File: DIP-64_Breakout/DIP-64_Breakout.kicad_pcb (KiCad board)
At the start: 2 copper layers, 42.2 x 85.1 mm, 6 parts, among them J1 DIP-64 Socket, J2 Left, J3 Right, J4 Decoupling Capacitor, J5 +5V In, J6 GND In

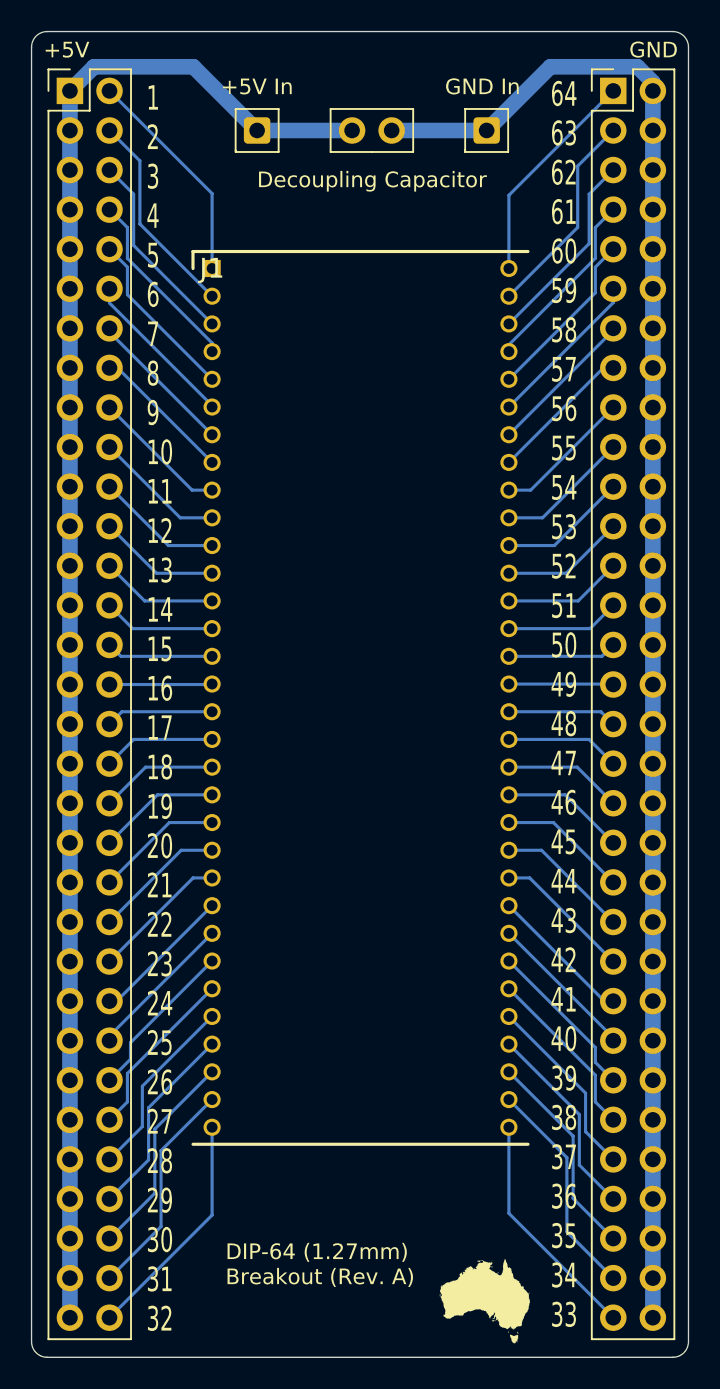
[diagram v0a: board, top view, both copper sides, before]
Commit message: Modified power input pins
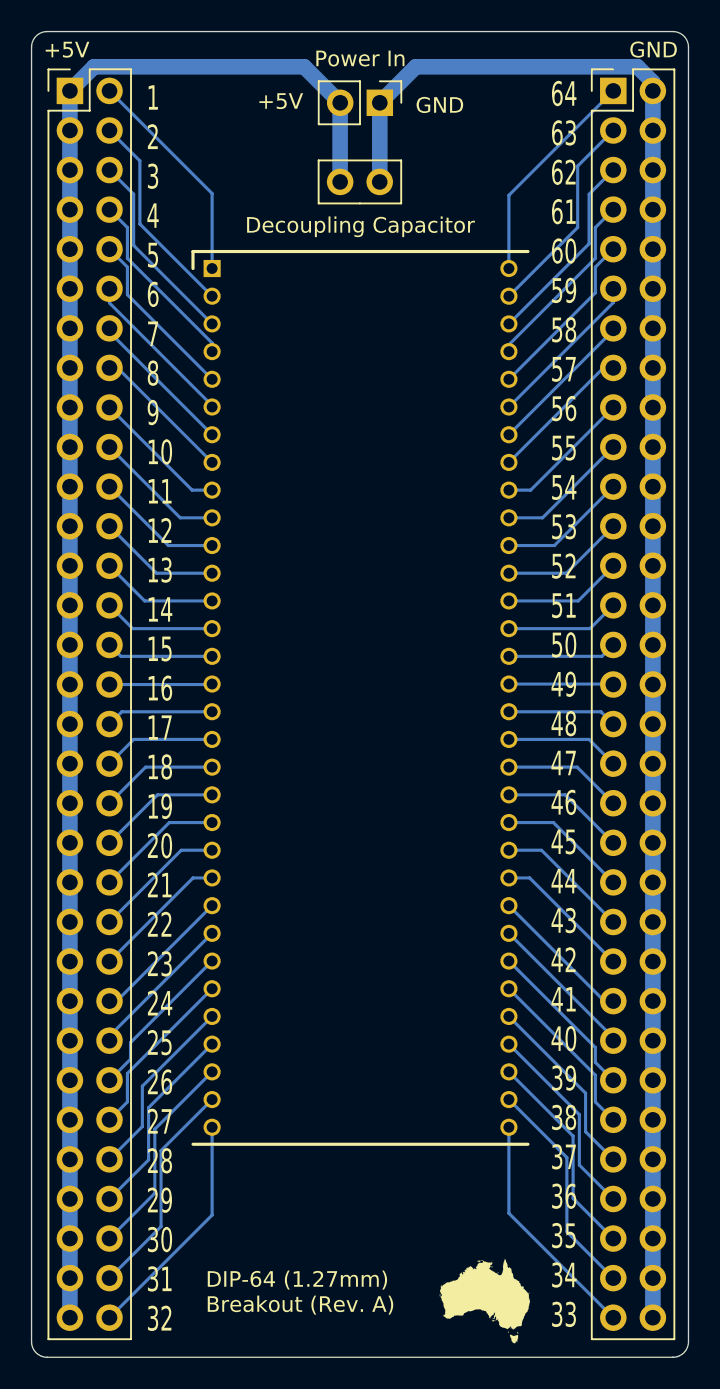
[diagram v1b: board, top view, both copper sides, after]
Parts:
- removed J6: GND In, Connector_PinHeader_2.54mm:PinHeader_1x01_P2.54mm_Vertical
- J5: value +5V In -> Power In; footprint Connector_PinHeader_2.54mm:PinHeader_1x01_P2.54mm_Vertical -> Connector_PinHeader_2.54mm:PinHeader_1x02_P2.54mm_Vertical
- moved J5 8.07 mm to (119.9, 52.3), turned to -90 degrees
- moved J4 3.39 mm to (117.3, 57.4)
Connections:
- J5 pad 1: +5V -> GND
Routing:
- net GND: track 98.2 -> 103.3 mm
- net +5V: track 99.2 -> 102.8 mm
